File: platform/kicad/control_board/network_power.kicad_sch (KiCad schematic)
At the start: 7 parts, among them J13 PJ-002A, J14 ROUTER 24V, J15 24V/5V OUT

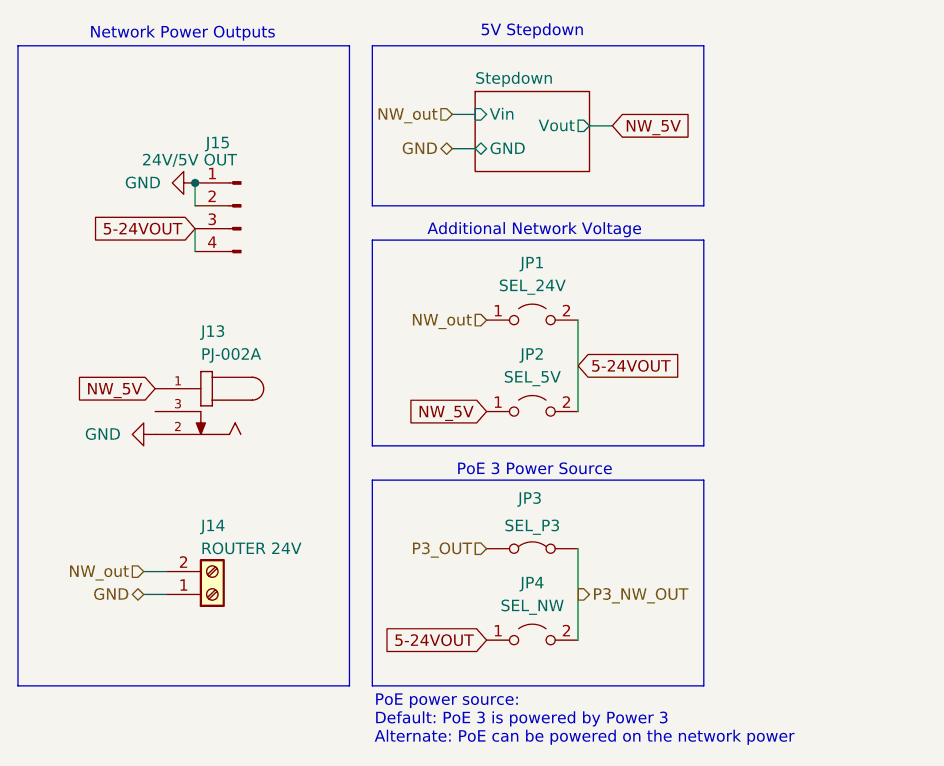
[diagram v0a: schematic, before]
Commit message: Control_PCB v4 revB: Finalised Design
This change updates the controller PCB to a finalised state, only requiring
finishing touches to be made for manufacturing.
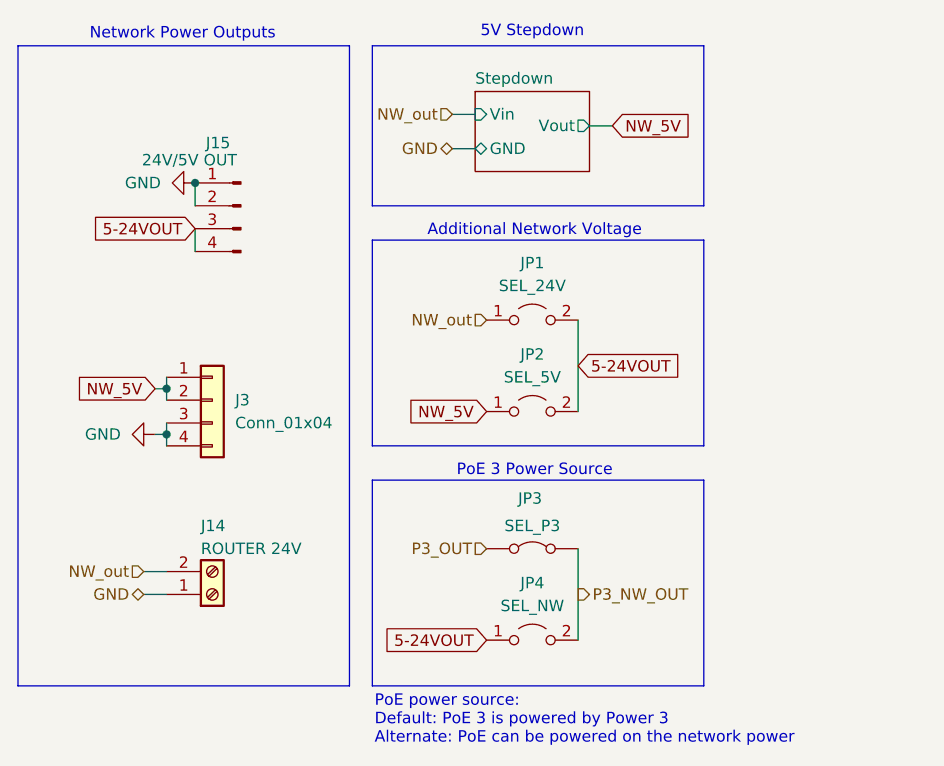
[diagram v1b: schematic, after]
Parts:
- removed J13: PJ-002A, AusOcean:CUI_PJ-002A, symbol AusOcean:PJ-002A
- added J3: Conn_01x04, Connector_JST:JST_XA_B04B-XASK-1_1x04_P2.50mm_Vertical, symbol Connector_Generic:Conn_01x04
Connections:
- net GND: now also J3.3 (Pin_3), J3.4 (Pin_4)
- net NW_5V: now also J3.1 (Pin_1), J3.2 (Pin_2)
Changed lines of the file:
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@@
 	(paper "A4")
+	(junction
+		(at 127 100.33)
+		(diameter 0)
+		(color 0 0 0 0)
+	)
+	(junction
+		(at 127 105.41)
+		(diameter 0)
+		(color 0 0 0 0)
+	)
 	(junction
 		(at 130.175 77.47)
@@
 	(wire
 		(pts
+			(xy 127 100.33) (xy 127 101.6)
+		)
+		(stroke
+			(width 0)
+			(type default)
+		)
+	)
+	(wire
+		(pts
 			(xy 130.175 85.09) (xy 130.175 82.55)
 		)
@@
 	(wire
 		(pts
+			(xy 127 104.14) (xy 127 105.41)
+		)
+		(stroke
+			(width 0)
+			(type default)
+		)
+	)
+	(wire
+		(pts
+			(xy 125.73 105.41) (xy 127 105.41)
+		)
+		(stroke
+			(width 0)
+			(type default)
+		)
+	)
+	(wire
+		(pts
 			(xy 124.46 120.65) (xy 127 120.65)
 		)
@@
 	(wire
 		(pts
+			(xy 127 105.41) (xy 127 106.68)
+		)
+		(stroke
+			(width 0)
+			(type default)
+		)
+	)
+	(wire
+		(pts
 			(xy 127 123.19) (xy 124.46 123.19)
 		)
@@
 	(wire
 		(pts
+			(xy 125.73 100.33) (xy 127 100.33)
+		)
+		(stroke
+			(width 0)
+			(type default)
+		)
+	)
+	(wire
+		(pts
 			(xy 130.175 80.01) (xy 130.175 77.47)
+		)
+		(stroke
+			(width 0)
+			(type default)
+		)
+	)
+	(wire
+		(pts
+			(xy 127 99.06) (xy 127 100.33)
 		)
 		(stroke
@@
 		(shape input)
 		(at 162.56 92.71 180)
-		(fields_autoplaced yes)
 		(effects
 			(font
@@
 		(shape bidirectional)
 		(at 158.75 73.66 180)
-		(fields_autoplaced yes)
 		(effects
 			(font
@@
 		(shape output)
 		(at 172.72 123.19 0)
-		(fields_autoplaced yes)
 		(effects
 			(font
@@
 		(shape input)
 		(at 162.56 118.11 180)
-		(fields_autoplaced yes)
 		(effects
 			(font
@@
 		(shape bidirectional)
 		(at 124.46 123.19 180)
-		(fields_autoplaced yes)
 		(effects
 			(font
@@
 		(shape input)
 		(at 158.75 69.85 180)
-		(fields_autoplaced yes)
 		(effects
 			(font
@@
 		(shape input)
 		(at 124.46 120.65 180)
-		(fields_autoplaced yes)
 		(effects
 			(font
@@
 	)
 	(symbol
-		(lib_id "AusOcean:PJ-002A")
-		(at 130.81 102.87 0)
-		(mirror y)
+		(lib_id "Connector_Generic:Conn_01x04")
+		(at 132.08 101.6 0)
 		(unit 1)
 		(exclude_from_sim no)
@@
 		(on_board yes)
 		(dnp no)
-		(property "Reference" "J13"
-			(at 130.81 93.98 0)
-			(effects
-				(font
-					(size 1.27 1.27)
-				)
-				(justify right)
-			)
-		)
-		(property "Value" "PJ-002A"
-			(at 130.81 96.52 0)
-			(effects
-				(font
-					(size 1.27 1.27)
-				)
-				(justify right)
-			)
-		)
-		(property "Footprint" "AusOcean:CUI_PJ-002A"
-			(at 130.81 102.87 0)
-			(effects
-				(font
-					(size 1.27 1.27)
-				)
-				(justify bottom)
-				(hide yes)
-			)
-		)
-		(property "Datasheet" ""
-			(at 130.81 102.87 0)
-			(effects
-				(font
-					(size 1.27 1.27)
-				)
-				(hide yes)
-			)
-		)
-		(property "Description" ""
-			(at 130.81 102.87 0)
-			(effects
-				(font
-					(size 1.27 1.27)
-				)
-				(hide yes)
-			)
-		)
-		(property "MANUFACTURER" "CUI INC"
-			(at 130.81 102.87 0)
-			(effects
-				(font
-					(size 1.27 1.27)
-				)
-				(justify bottom)
-				(hide yes)
-			)
-		)
-		(property "STANDARD" "Manufacturer recommendations"
-			(at 130.81 102.87 0)
-			(effects
-				(font
-					(size 1.27 1.27)
-				)
-				(justify bottom)
-				(hide yes)
-			)
+		(fields_autoplaced yes)
+		(property "Reference" "J3"
+			(at 134.62 101.6 0)
+			(effects
+				(font
+					(size 1.27 1.27)
+				)
+				(justify left)
+			)
+		)
+		(property "Value" "Conn_01x04"
+			(at 134.62 104.14 0)
+			(effects
+				(font
+					(size 1.27 1.27)
+				)
+				(justify left)
+			)
+		)
+		(property "Footprint" "Connector_JST:JST_XA_B04B-XASK-1_1x04_P2.50mm_Vertical"
+			(at 132.08 101.6 0)
+			(effects
+				(font
+					(size 1.27 1.27)
+				)
+				(hide yes)
+			)
+		)
+		(property "Datasheet" "~"
+			(at 132.08 101.6 0)
+			(effects
+				(font
+					(size 1.27 1.27)
+				)
+				(hide yes)
+			)
+		)
+		(property "Description" "Generic connector, single row, 01x04, script generated (kicad-library-utils/schlib/autogen/connector/)"
+			(at 132.08 101.6 0)
+			(effects
+				(font
+					(size 1.27 1.27)
+				)
+				(hide yes)
+			)
+		)
+		(pin "4"
+		)
+		(pin "2"
 		)
 		(pin "3"
@@
 		(pin "1"
 		)
-		(pin "2"
-		)
 		(instances
-			(project "control_board"
+			(project ""
 				(path "/bacab6d6-2a0b-4208-9256-c826bcae29b3/5c908c9f-4997-4e6c-84f5-82f8ec5dbea2"
-					(reference "J13")
+					(reference "J3")
 					(unit 1)
 				)
